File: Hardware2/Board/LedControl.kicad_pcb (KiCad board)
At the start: 2 copper layers, 70 x 52 mm, 148 parts, among them J2 Jumper, J3 Jumper, J4 Jumper, J5 Jumper, J7 Jumper, P1 USB_OTG, P10 Micro_SD, P11 Header, P12 DISPLAY, P13 TP, P14 TMM-103-03-G-S, P15 TP, P16 TP, P17 2059-302, P18 CONN_01X03, P19 TP, P2 2059-302, P20 TP, P21 TP, P22 TP, P23 TP, P24 2060-452, P25 2060-452, P26 TP, P27 TP, P28 2060-452, P29 2059-302, P3 2059-302, P30 LED_Strip, P31 LED_Strip, P32 TP, P33 TP, P34 TP, P35 2060-452, P36 TP, P38 TP, P39 TP, P4 2059-302, P40 TP, P41 TP, P42 TP, P43 TP, P44 TP, P5 2059-302, P6 2059-302, P7 2059-302, P8 2059-302, P9 2059-302, Q1 DMG1012UW, Q2 DMG1012UW, SW1 PEC12R-4215F-S0024, SW2 PEC12R-4215F-S0024, U1 STM32L433CCUx, U10 SP485CN, U2 SN65HVD230, U3 SP485CN, U4 SP485CN, U5 TPS82130, U6 LP2985IM5-3.3, U7 TPS82130, U8 SP485CN, U9 TPS82130, X1 IQXO/7X

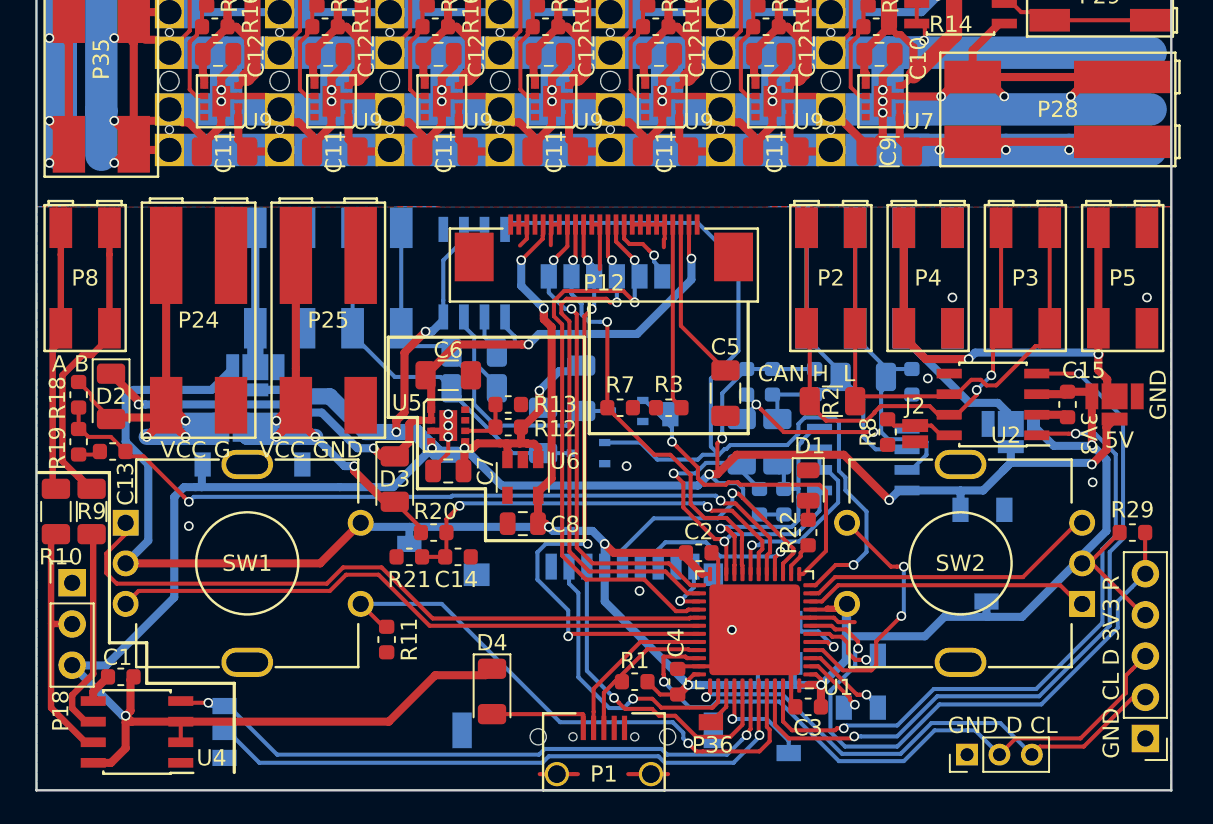
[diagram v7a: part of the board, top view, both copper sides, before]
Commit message: add rfid and speaker
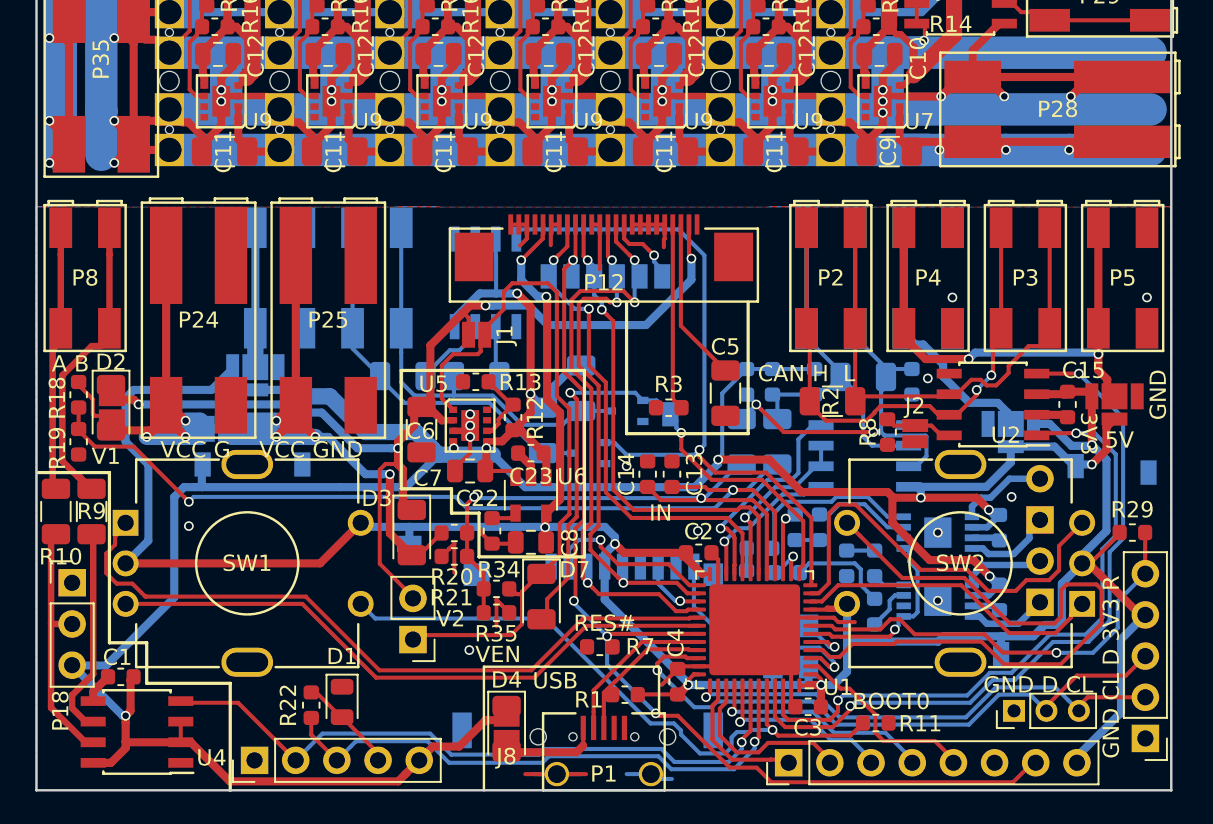
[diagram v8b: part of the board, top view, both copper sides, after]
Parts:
- removed P34, P36, P39, P41, P42, P43: TP, LedControl:Pad
- added C18: 100p, Capacitor_SMD:C_0603_1608Metric, B.Cu at (111.8, 119.8)
- added C19: 100p, Capacitor_SMD:C_0603_1608Metric, B.Cu at (108.8, 123.2)
- added C20: 100n, Capacitor_SMD:C_0603_1608Metric, B.Cu at (124.4, 119.8)
- added C21: 100n, Capacitor_SMD:C_0603_1608Metric, B.Cu at (124.4, 124.1)
- added C22: 10n, Capacitor_SMD:C_0603_1608Metric, F.Cu at (93.1, 120.0)
- added C23: 100n, Capacitor_SMD:C_0603_1608Metric, F.Cu at (95.5, 115.2)
- added D7: SD1206S020S1R0, Diode_SMD:D_1206_3216Metric, F.Cu at (96.2, 124.0)
- added J1: Jumper, LedControl:Jumper, F.Cu at (92.2, 107.9)
- added J6: Jumper, LedControl:Jumper, F.Cu at (69.7, 112.4)
- added J8: Jumper, LedControl:Jumper, F.Cu at (94.0, 132.2)
- added P37: Header, Connector_PinHeader_2.54mm:PinHeader_1x08_P2.54mm_Vertical, F.Cu at (111.4, 134.3)
- added P45: Header, Connector_PinHeader_2.54mm:PinHeader_1x02_P2.54mm_Vertical, B.Cu at (126.9, 124.4)
- added P46: Header, Connector_PinHeader_2.54mm:PinHeader_1x02_P2.54mm_Vertical, B.Cu at (126.9, 119.3)
- added R30: 150k, Resistor_SMD:R_0603_1608Metric, B.Cu at (116.7, 125.0)
- added R31: 150k, Resistor_SMD:R_0603_1608Metric, B.Cu at (116.7, 122.0)
- added R32: 150k, Resistor_SMD:R_0603_1608Metric, B.Cu at (113.3, 119.8)
- added R33: 150k, Resistor_SMD:R_0603_1608Metric, B.Cu at (109.6, 121.1)
- added R34: 52k3, Resistor_SMD:R_0603_1608Metric, F.Cu at (93.4, 123.6)
- added R35: 10k, Resistor_SMD:R_0603_1608Metric, F.Cu at (93.4, 125.0)
- added U11: TPA2005, Package_SO:MSOP-8-1EP_3x3mm_P0.65mm_EP1.68x1.88mm, B.Cu at (120.6, 124.3)
- added U12: TPA2005, Package_SO:MSOP-8-1EP_3x3mm_P0.65mm_EP1.68x1.88mm, B.Cu at (120.6, 120.1)
- C16, C17: value 100n -> 100p
- P1: value USB_OTG -> Micro_USB
- P16: value TP -> Header; footprint LedControl:Pad -> Connector_PinHeader_2.54mm:PinHeader_1x05_P2.54mm_Vertical; moved to F.Cu
- P19: value TP -> Header; footprint LedControl:Pad -> Connector_PinHeader_2.54mm:PinHeader_1x02_P2.54mm_Vertical; moved to F.Cu
- moved P16 39.0 mm to (78.5, 134.2)
- moved C13 34.5 mm to (104.2, 116.5), turned to 90 degrees
- moved R22 32.4 mm to (82.0, 130.8)
- moved D1 31.7 mm to (83.8, 130.6)
- moved R11 30.6 mm to (116.8, 131.8), turned to 180 degrees
- moved P19 26.9 mm to (88.2, 126.7), turned to 180 degrees
- moved R7 14.8 mm to (99.8, 127.2), turned to 0 degrees
- moved C14 12.8 mm to (102.7, 116.5), turned to 90 degrees
- moved P27 9.19 mm to (133.6, 116.4)
- moved P20 7.60 mm to (129.1, 116.0)
- moved C17 6.58 mm to (115.0, 122.0), turned to 270 degrees
- moved R24 4.46 mm to (87.6, 110.5)
- moved C16 4.38 mm to (111.3, 122.6), turned to 180 degrees
- moved P14 3.96 mm to (125.3, 131.1)
- moved C6 3.73 mm to (88.8, 113.8), turned to 270 degrees
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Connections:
- net Net-(P13-Pad1) renamed OUT2
- net STRIP2_TX renamed STRIP2_TX_OUT1
- C11 pad 1: (no net) -> Net-(C11-Pad1) (x4)
- C11 pad 2: (no net) -> GNDD (x4)
- C12 pad 1: (no net) -> +5VD (x4)
- C12 pad 2: (no net) -> GNDD (x4)
- C13 pad 1: U1 -> IN1
- C14 pad 1: U2 -> IN2
- C16 pad 1: +5V -> Net-(C16-Pad1)
- C16 pad 2: RS485_TX -> AUDIO1
- C17 pad 1: +5V -> Net-(C17-Pad1)
- C17 pad 2: RS485_RX -> GND
- P10 pad 3: SD_MOSI -> DISP_SD_MOSI
- P10 pad 5: SD_SCK -> DISP_SD_SCK
- P12 pad 13: DISP_SCK -> DISP_SD_SCK
- P12 pad 14: DISP_MOSI -> DISP_SD_MOSI
- P12 pad 9: DISP_RES# -> DISP_RFID_RES#
- P16 pad 1: Net-(P16-Pad1) -> GND
- P19 pad 1: Net-(P19-Pad1) -> /Power/EN
- P31 pad 1: (no net) -> Net-(C11-Pad1) (x4)
- P31 pad 2: (no net) -> GNDD (x4)
- P31 pad 3: (no net) -> GNDD (x4)
- P31 pad 4: (no net) -> Net-(P30-Pad4) (x4)
- P31 pad 5: (no net) -> +5VD (x4)
- P38 pad 1: DISP_SCK -> DISP_SD_SCK
- P40 pad 1: DISP_MOSI -> DISP_SD_MOSI
- P44 pad 1: DISP_RES# -> DISP_RFID_RES#
- R16 pad 1: (no net) -> +5VD (x4)
- R16 pad 2: (no net) -> Net-(R16-Pad2) (x4)
- R17 pad 1: (no net) -> Net-(R16-Pad2) (x4)
- R17 pad 2: (no net) -> GNDD (x4)
- R18 pad 2: U1 -> IN1
- R19 pad 1: U1 -> IN1
- R20 pad 2: U2 -> IN2
- R21 pad 1: U2 -> IN2
- R22 pad 1: DEBUG_LED -> LED_TTY_RX
- R26 pad 1: RS485_TX -> IN1
- R28 pad 1: RS485_RX -> IN2
- R7 pad 2: DISP_RES# -> DISP_RFID_RES#
- U1 pad 14: DEBUG_LED -> AUDIO1
- U1 pad 15: SD_SCK -> AUDIO2
- U1 pad 16: SD_MISO -> IN1
- U1 pad 17: U1 -> IN2
- U1 pad 18: U2 -> DISP_D_C#
- U1 pad 2: Net-(P19-Pad1) -> RFID_IRQ
- U1 pad 20: DISP_RES# -> DISP_NSS
- U1 pad 25: DISP_NSS -> SD_NSS
- U1 pad 26: DISP_SCK -> DISP_SD_SCK
- U1 pad 27: SD_DET -> SD_MISO
- U1 pad 28: DISP_MOSI -> DISP_SD_MOSI
- U1 pad 3: Net-(P34-Pad1) -> SD_DET
- U1 pad 31: DISP_D_C# -> DISP_RFID_RES#
- U1 pad 38: SD_NSS -> RFID_NSS
- U1 pad 39: Net-(P36-Pad1) -> RFID_SCK
- U1 pad 40: Net-(P39-Pad1) -> RFID_MISO
- U1 pad 41: SD_MOSI -> RFID_MOSI
- U1 pad 43: TTY_RX -> LED_TTY_RX
- U1 pad 6: Net-(P16-Pad1) -> SHUTDOWN
- U5 pad 1: VCC -> /Power/EN
- U9 pad 1: (no net) -> Net-(C11-Pad1) (x4)
- U9 pad 2: (no net) -> Net-(C11-Pad1) (x4)
- U9 pad 3: (no net) -> GNDD (x4)
- U9 pad 4: (no net) -> +5VD (x4)
- U9 pad 5: (no net) -> +5VD (x4)
- U9 pad 6: (no net) -> Net-(R16-Pad2) (x4)
- U9 pad 7: (no net) -> Net-(U9-Pad7) (x4)
- U9 pad 8: (no net) -> Net-(U9-Pad8) (x4)
- U9 pad 9: (no net) -> GNDD (x4)
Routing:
- net DISP_RFID_RES#: track 0.00 -> 66.6 mm, vias 0 -> 4
- net IN1: track 0.00 -> 58.7 mm, vias 0 -> 2
- net U1: track 49.4 -> 0.00 mm, vias 2 -> 0
- net /Power/EN: track 0.00 -> 43.9 mm
- net TTY_RX: track 38.0 -> 0.00 mm, vias 1 -> 0
- net IN2: track 0.00 -> 37.1 mm, vias 0 -> 2
- net DISP_SD_MOSI: track 0.00 -> 36.9 mm, vias 0 -> 3
- net DISP_MOSI: track 36.9 -> 0.00 mm, vias 2 -> 0
- net LED_TTY_RX: track 0.00 -> 35.1 mm, vias 0 -> 1
- net DISP_SCK: track 33.2 -> 0.00 mm, vias 2 -> 0
- net DISP_SD_SCK: track 0.00 -> 32.3 mm, vias 0 -> 3
- net DISP_RES#: track 28.1 -> 0.00 mm, vias 2 -> 0
- net U2: track 26.8 -> 0.00 mm, vias 2 -> 0
- net Net-(R16-Pad2): track 13.4 -> 40.1 mm
- net (no net): track 492.4 -> 465.7 mm
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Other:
- board text added: "BOOT0"
- board text added: "IN"
- board text added: "RES#"
- board text added: "RS485/IN B A"
- board text added: "STRIP2/OUT B A GND 5V"
- board text added: "USB"
- board text added: "V1"
- board text added: "V2"
- board text added: "VEN"
- board text removed: "RS485 B A"
- board text removed: "STRIP2 B A GND 5V"
